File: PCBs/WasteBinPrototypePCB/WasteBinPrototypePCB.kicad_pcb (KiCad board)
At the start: 2 copper layers, 31 parts, among them J1 Jack-DC 12V, J2 Conn_01x10_Male, J3 Conn_01x06_Male, J4 SM04B-SRSS-TB(LF)(SN), Q1 MMBT3904, Q2 IRL540NSTRLPBF, U1 PC817, U2 TLV1117-50, U3 ESP32-C3-DEVKITC-02, U4 A1301EUA-T

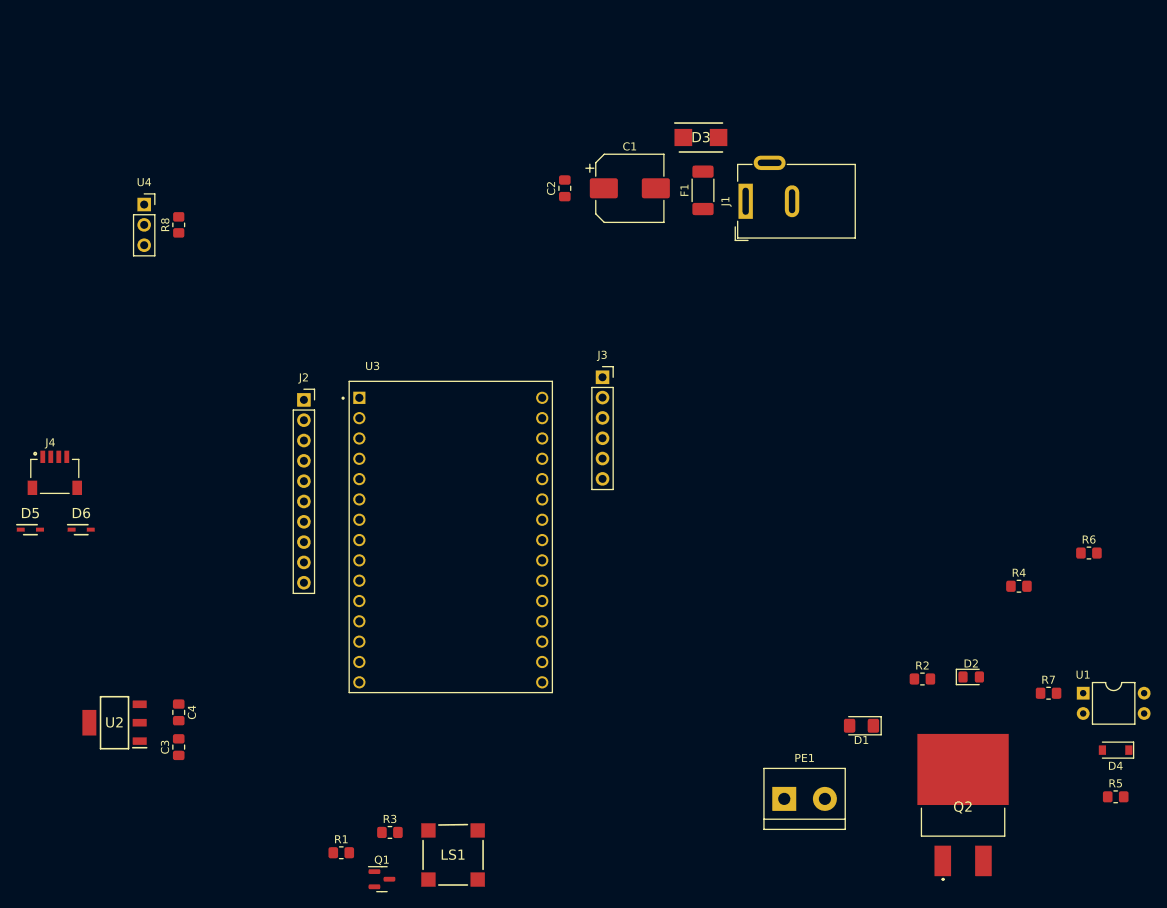
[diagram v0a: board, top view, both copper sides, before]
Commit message: created pcb board outline, layed out components and starting retouing wires.
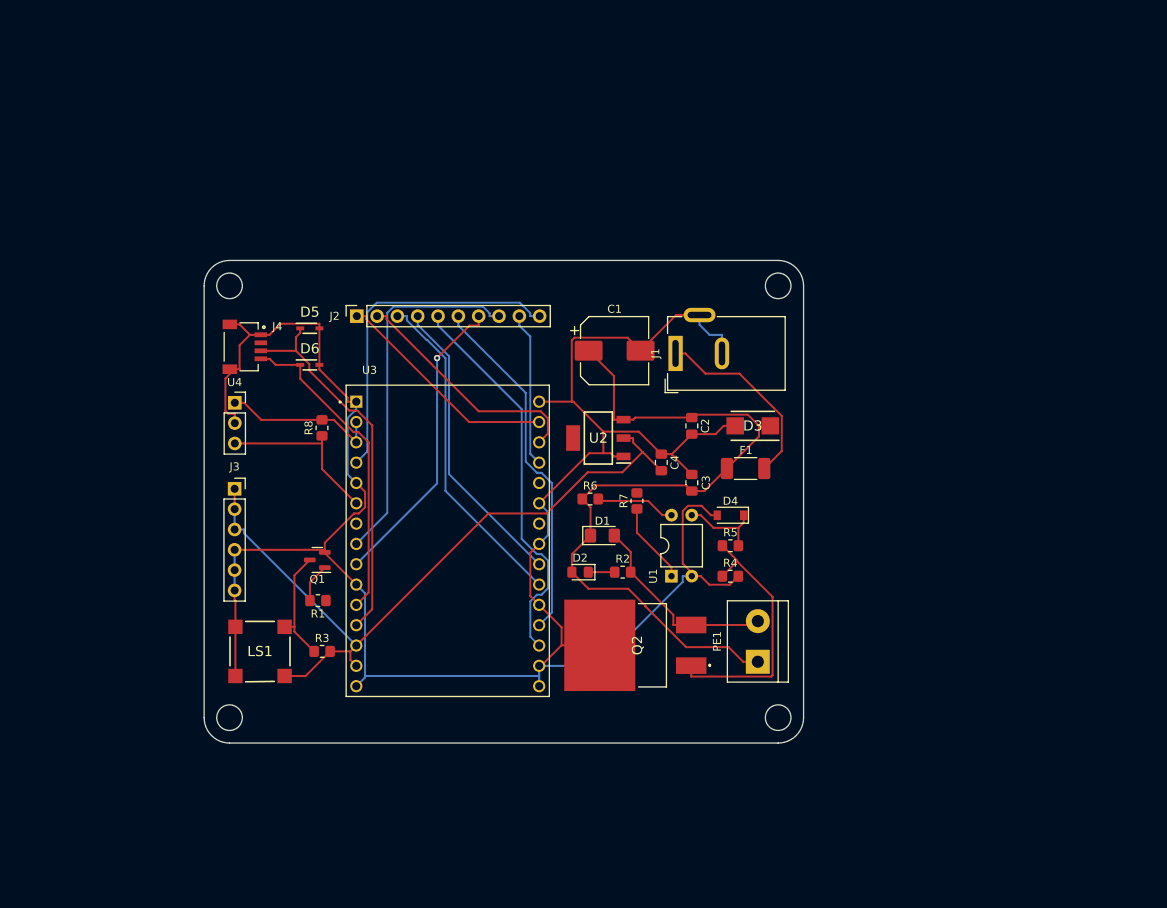
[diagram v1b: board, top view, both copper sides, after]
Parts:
- added H1: MountingHole_Pad, MountingHole:MountingHole_3.2mm_M3, F.Cu at (158.8, 67.3)
- added H2: MountingHole_Pad, MountingHole:MountingHole_3.2mm_M3, F.Cu at (158.8, 121.3)
- added H3: MountingHole_Pad, MountingHole:MountingHole_3.2mm_M3, F.Cu at (90.2, 67.3)
- added H4: MountingHole_Pad, MountingHole:MountingHole_3.2mm_M3, F.Cu at (90.2, 121.3)
- moved C3 72.1 mm to (148.0, 91.9)
- moved U2 70.2 mm to (136.3, 86.3)
- moved C4 67.9 mm to (144.1, 89.4)
- moved R6 62.7 mm to (135.3, 94.0)
- moved R5 57.5 mm to (152.8, 99.8)
- moved R7 56.8 mm to (141.1, 94.2), turned to 90 degrees
- moved D4 56.4 mm to (152.8, 96.0)
- moved U1 53.5 mm to (145.4, 103.6), turned to 90 degrees
- moved D2 50.6 mm to (134.0, 103.1), turned to 180 degrees
- moved J3 48.1 mm to (90.8, 92.7)
- moved Q2 44.6 mm to (143.1, 112.2), turned to 90 degrees
- moved D5 43.1 mm to (100.2, 72.6)
- moved Q1 40.7 mm to (101.1, 101.6), turned to 180 degrees
- moved D1 40.2 mm to (136.8, 98.5), turned to 0 degrees
- moved R2 39.8 mm to (139.3, 103.1)
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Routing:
- net GND: track 0.00 -> 287.7 mm
- net 12V: track 0.00 -> 96.0 mm
- net 5V: track 0.00 -> 91.8 mm
- net GPIO19: track 0.00 -> 48.9 mm
- net SCL: track 0.00 -> 47.1 mm
- net GPIO6: track 0.00 -> 45.5 mm
- net GPIO18: track 0.00 -> 44.5 mm
- net RST: track 0.00 -> 42.3 mm
- net GPIO21: track 0.00 -> 41.6 mm
- net SDA: track 0.00 -> 39.8 mm
- net GPIO7: track 0.00 -> 38.0 mm, vias 0 -> 1
- net GPIO20: track 0.00 -> 37.4 mm
- net Net-(Q2-Pad1): track 0.00 -> 33.0 mm
- net GPIO28: track 0.00 -> 30.3 mm
- net GPIO29: track 0.00 -> 28.5 mm
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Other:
- board outline added: 74.9 x 60.3 mm

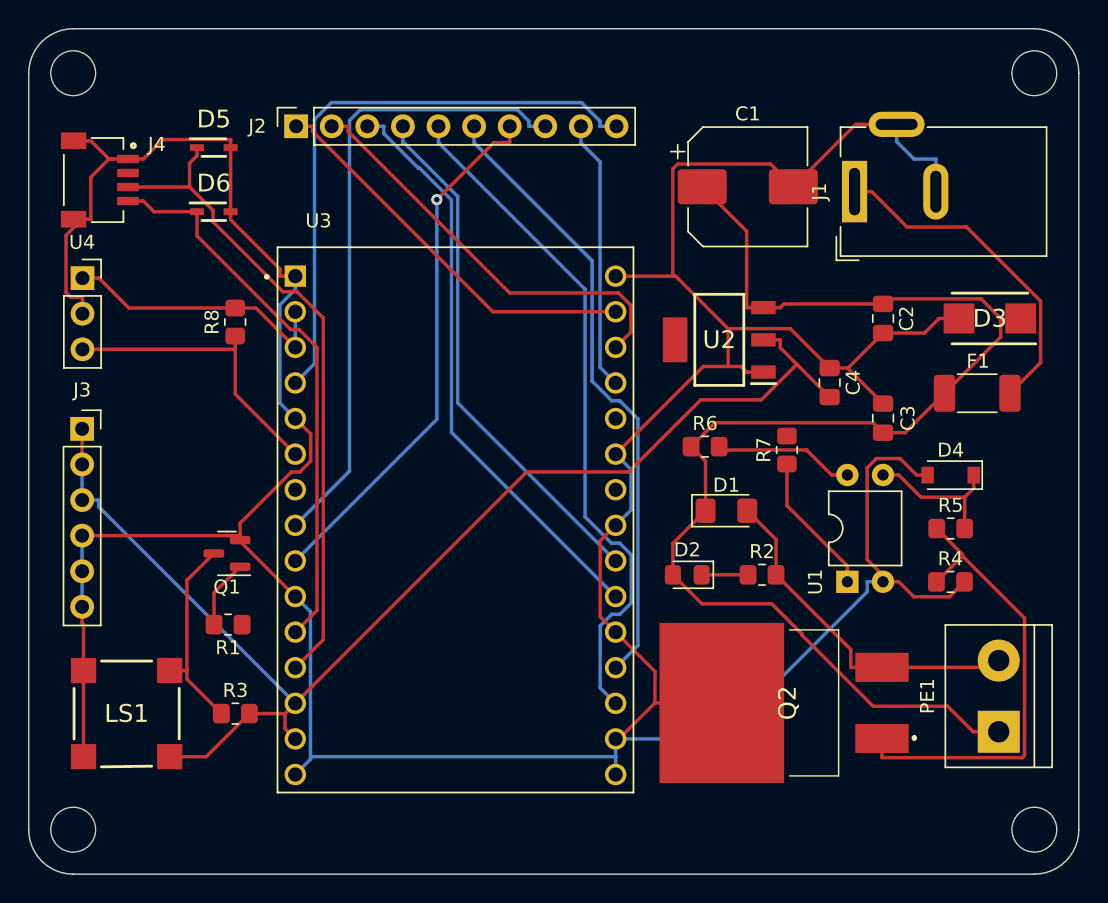
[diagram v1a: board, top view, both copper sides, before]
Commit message: finished wiring and added silkscreen.
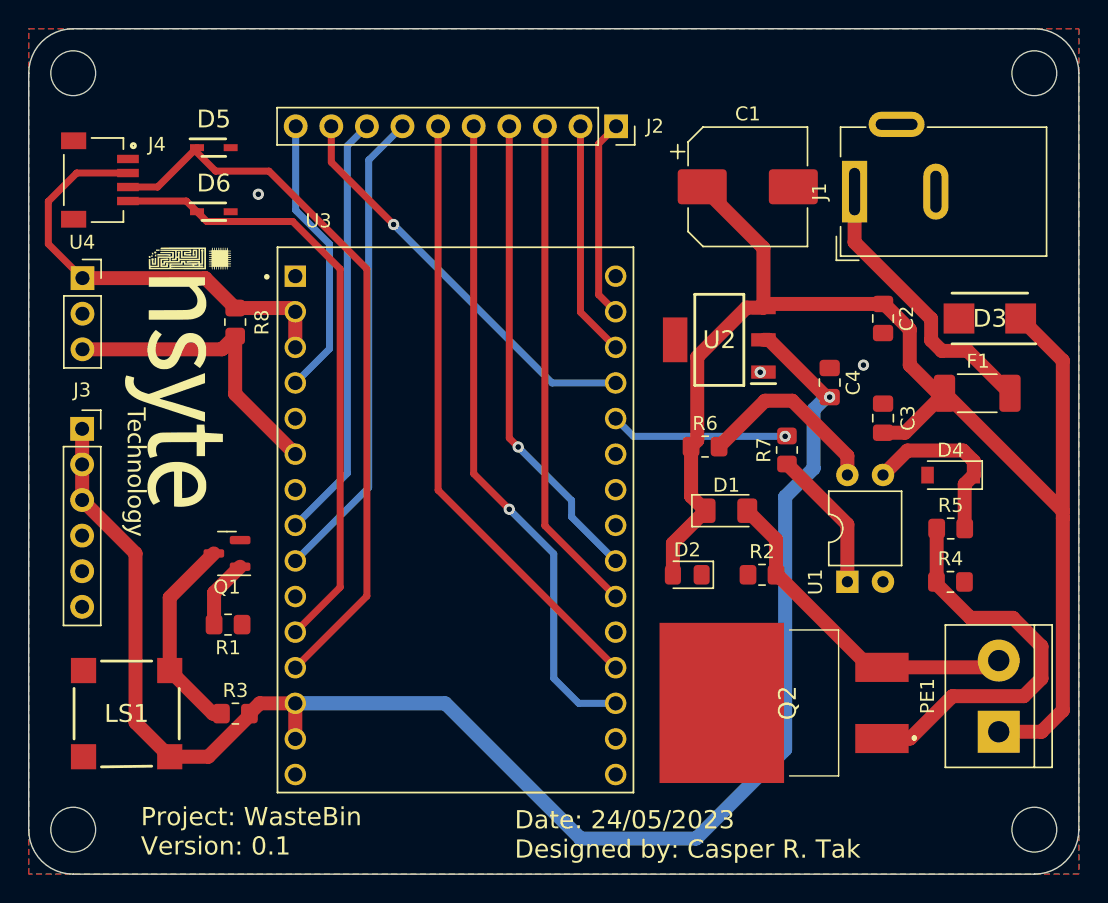
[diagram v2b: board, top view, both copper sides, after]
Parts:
- added G***: LOGO, LOGO, F.Cu at (96.7, 94.7)
- added G***: LOGO, LOGO, B.Cu at (116.8, 91.0)
- moved J2 22.8 mm to (128.9, 71.1), turned to -90 degrees
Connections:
- J4 pad 2: 3.3V+ -> 3.3V
- R7 pad 2: PWM -> PeltierCtrl
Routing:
- net GND: track 287.7 -> 0.00 mm, vias 0 -> 3
- net 5V: track 91.8 -> 114.4 mm, vias 0 -> 1
- net RST: track 42.3 -> 20.3 mm
- net GPIO6: track 45.5 -> 30.6 mm
- net GPIO29: track 28.5 -> 14.3 mm
- net GPIO28: track 30.3 -> 16.8 mm
- net PeltierCtrl: track 0.00 -> 12.6 mm, vias 0 -> 1
- net 3.3V: track 19.8 -> 31.7 mm
- net GPIO2: track 19.3 -> 29.4 mm, vias 0 -> 1
- net 12V: track 96.0 -> 102.9 mm
- net GPIO21: track 41.6 -> 35.6 mm
- net SCL: track 47.1 -> 52.5 mm
- net SDA: track 39.8 -> 44.4 mm
- net Net-(Q2-Pad1): track 33.0 -> 28.7 mm
- net Net-(F1-Pad1): track 24.0 -> 20.1 mm
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- added copper zone on B.Cu, net GND
- added copper zone on F.Cu, net GND
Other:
- board text added: "Date: 24/05/2023 Designed by: Casper R. Tak"
- board text added: "Project: WasteBin Version: 0.1"

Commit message: finished V0.1, waiting for feedback
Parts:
- moved PE1 38.2 mm to (133.2, 83.8)
- moved C2 38.0 mm to (125.4, 54.3)
- moved C3 38.0 mm to (125.4, 61.4)
- moved D1 38.0 mm to (114.2, 68.0)
- moved D2 38.0 mm to (111.4, 72.6)
- moved D3 38.0 mm to (133.0, 54.3)
- moved D5 38.0 mm to (77.6, 42.1)
- moved D6 38.0 mm to (77.6, 46.7)
- moved G*** 38.0 mm to (74.1, 64.2)
- moved J3 38.0 mm to (68.2, 62.2)
- moved LS1 38.0 mm to (71.4, 82.5)
- moved Q1 38.0 mm to (78.5, 71.1)
- moved R1 38.0 mm to (78.6, 76.1)
- moved R7 38.0 mm to (118.5, 63.7)
- moved R8 38.0 mm to (79.1, 54.6)
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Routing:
- net GND: vias 3 -> 5
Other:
- outline, holes or cut-outs redrawn
- board text added: "12V DC input"
- board text added: "18"
- board text added: "19"
- board text added: "2"
- board text added: "20"
- board text added: "21"
- board text added: "28"
- board text added: "29"
- board text added: "3.3V"
- board text added: "5V"
- board text added: "6"
- board text added: "7"
- board text added: "ESP32-C3-DevKitC-02V1.1"
- board text added: "GND"
- board text added: "GPIO"
- board text added: "I2C"
- board text added: "LidP"
- board text added: "Peltier"
- board text added: "rst"

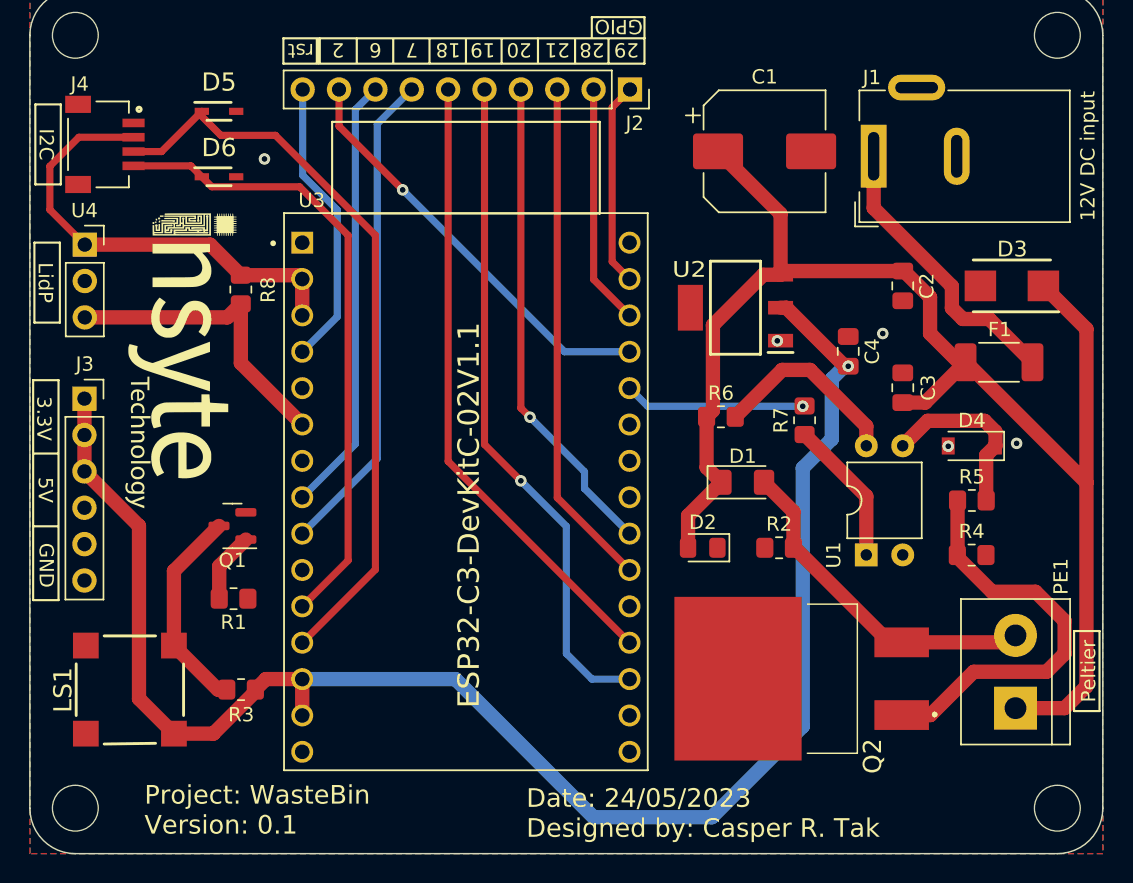
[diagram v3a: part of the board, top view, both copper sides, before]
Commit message: applied rounded tracks design
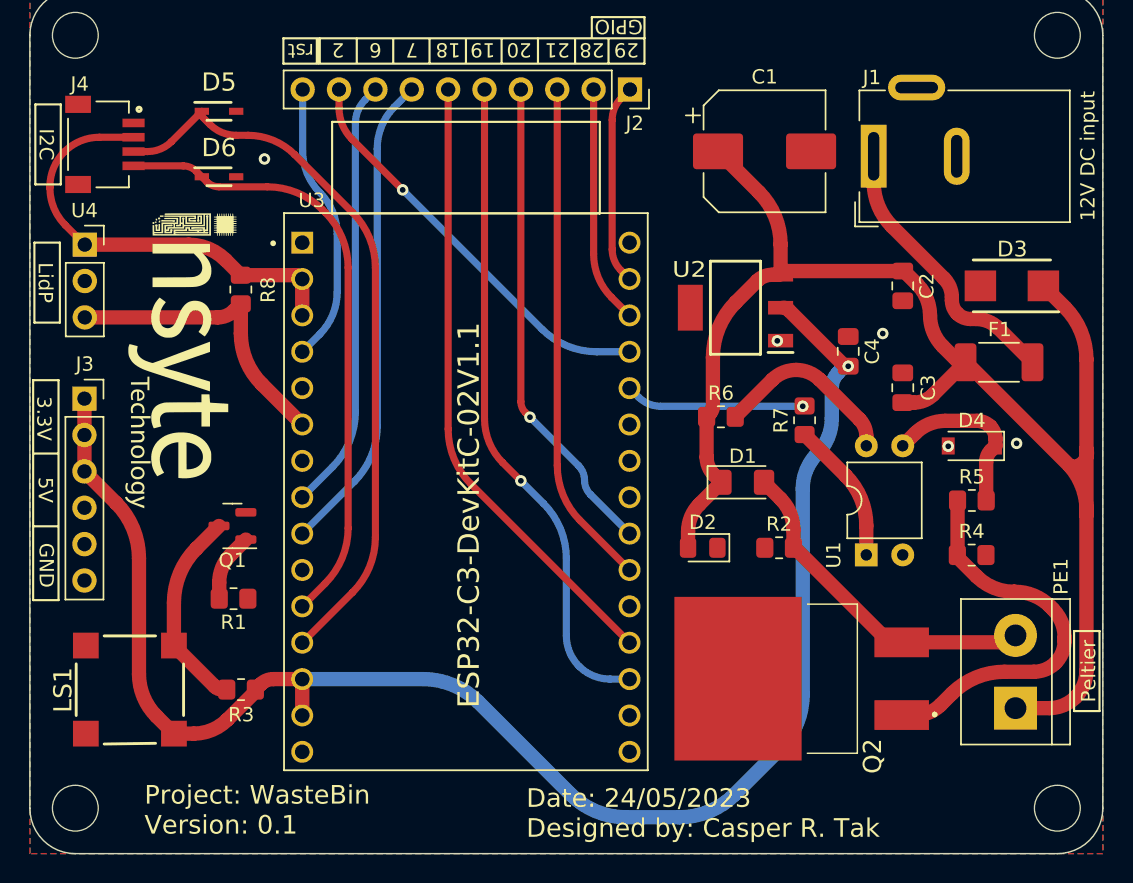
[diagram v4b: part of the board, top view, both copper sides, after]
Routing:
- net 5V: track 114.4 -> 111.8 mm
- net 12V: track 103.3 -> 105.7 mm
- net Net-(Q2-Pad1): track 28.7 -> 27.7 mm
- net SDA: track 44.2 -> 43.3 mm
- net GPIO19: track 46.9 -> 46.2 mm
- net 3.3V: track 31.9 -> 31.2 mm
- net SCL: track 52.3 -> 51.6 mm
- net RST: track 20.3 -> 19.7 mm
- net Net-(F1-Pad1): track 20.1 -> 19.5 mm
